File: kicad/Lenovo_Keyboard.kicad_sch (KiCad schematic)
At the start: 5 parts, among them J1 Conn_01x34_Pin, J2 Conn_01x04_Socket, J3 Conn_01x04_Socket

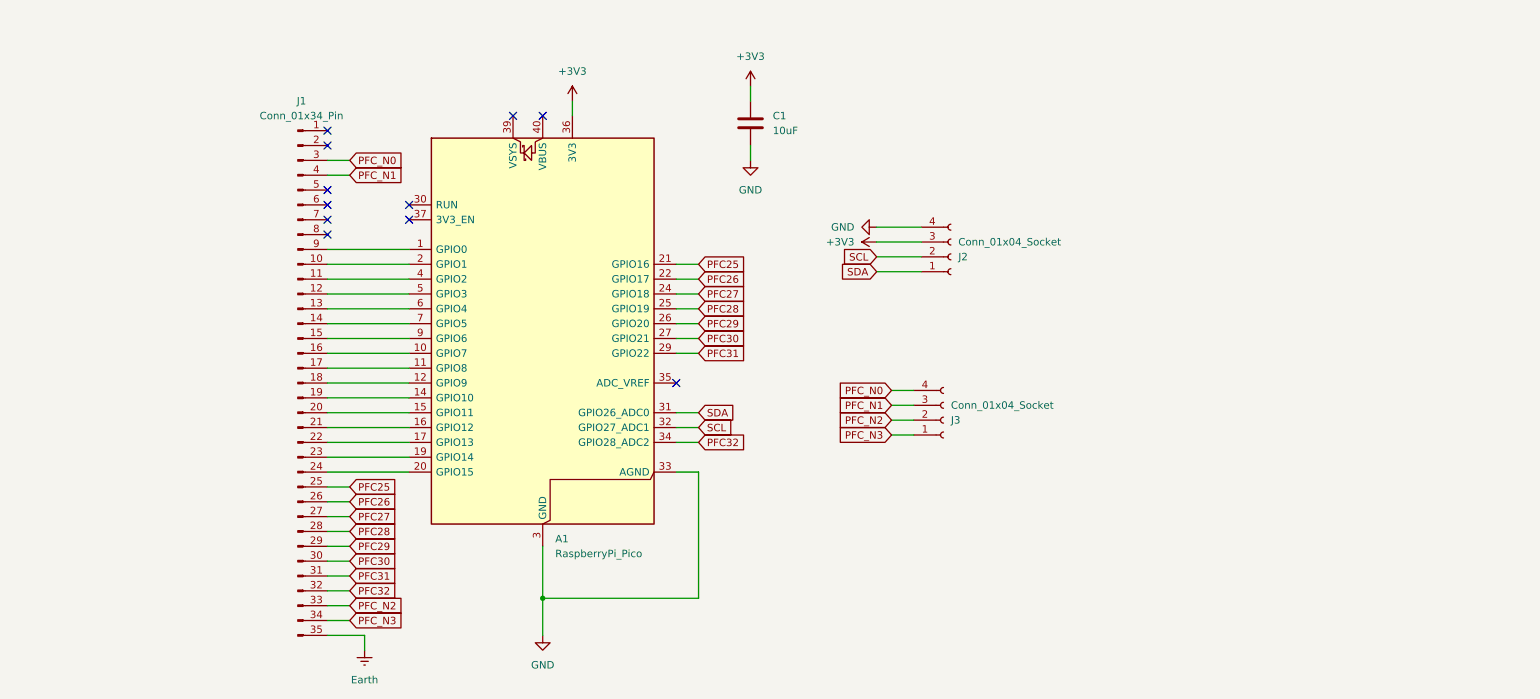
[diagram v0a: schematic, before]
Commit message: SOIC-16 version
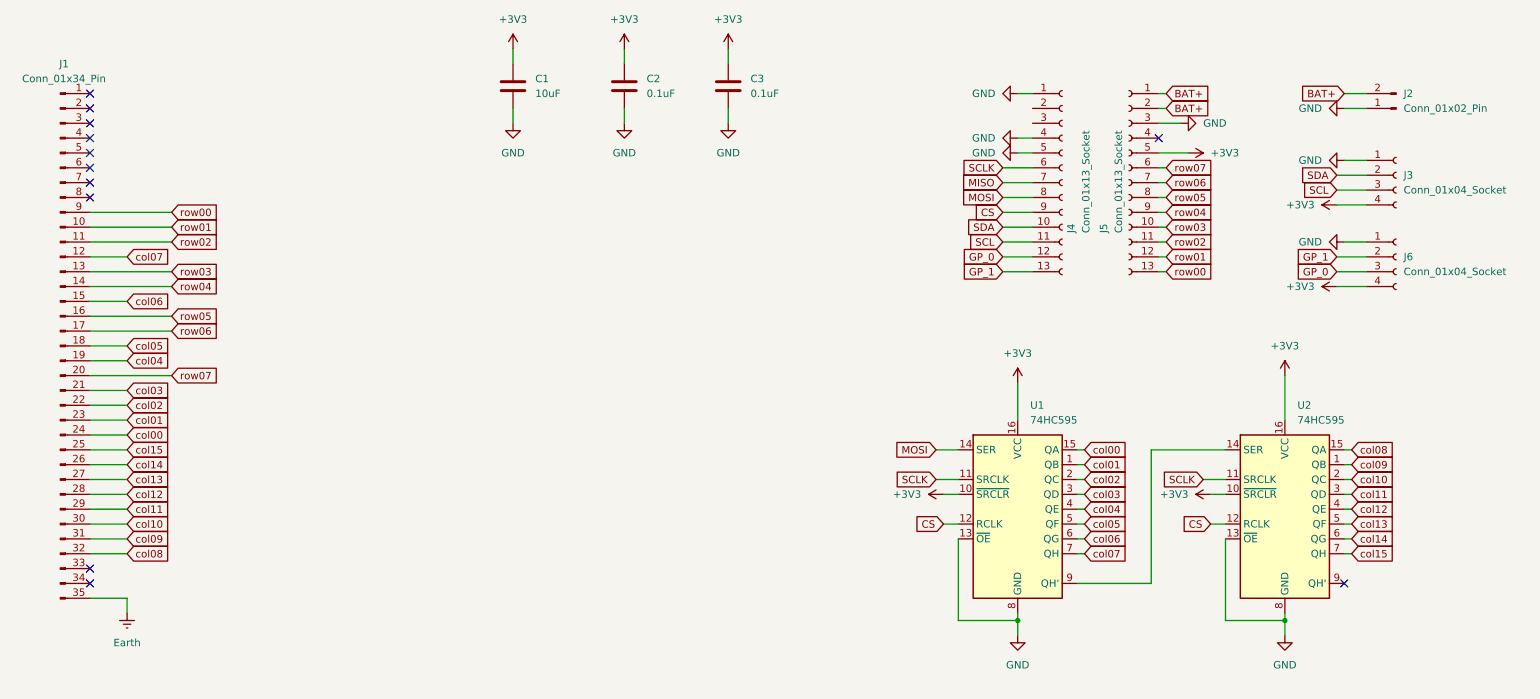
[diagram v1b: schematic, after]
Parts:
- removed A1: RaspberryPi_Pico, Module:RaspberryPi_Pico_Common_SMD, symbol MCU_Module:RaspberryPi_Pico
- removed J2: Conn_01x04_Socket, Connector_JST:JST_PH_S4B-PH-K_1x04_P2.00mm_Horizontal, symbol Connector:Conn_01x04_Socket
- added C2, C3: 0.1uF, Capacitor_SMD:C_0805_2012Metric_Pad1.18x1.45mm_HandSolder, symbol Device:C
- added J2: Conn_01x02_Pin, Connector_JST:JST_PH_S2B-PH-K_1x02_P2.00mm_Horizontal, symbol Connector:Conn_01x02_Pin
- added J4, J5: Conn_01x13_Socket, Connector_PinSocket_2.54mm:PinSocket_1x13_P2.54mm_Vertical, symbol Connector:Conn_01x13_Socket
- added J6: Conn_01x04_Socket, Connector_JST:JST_PH_S4B-PH-K_1x04_P2.00mm_Horizontal, symbol Connector:Conn_01x04_Socket
- added U1, U2: 74HC595, Package_SO:SOIC-16W_7.5x10.3mm_P1.27mm, symbol 74xx:74HC595
- J3: footprint Connector_JST:JST_ZH_B4B-ZR_1x04_P1.50mm_Vertical -> Connector_JST:JST_PH_S4B-PH-K_1x04_P2.00mm_Horizontal
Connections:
- net +3V3: now also J3.4 (Pin_4), C2.1, C3.1, J5.5 (Pin_5), J6.4 (Pin_4), U1.10 (~{SRCLR}), U1.16 (VCC), U2.10 (~{SRCLR}), U2.16 (VCC)
- net GND: now also J3.1 (Pin_1), C2.2, C3.2, J2.1 (Pin_1), J4.1 (Pin_1), J4.4 (Pin_4), J4.5 (Pin_5), J5.3 (Pin_3), J6.1 (Pin_1), U1.13 (~{OE}), U1.8 (GND), U2.13 (~{OE}), U2.8 (GND)
- net SCL: now also J3.3 (Pin_3), J4.11 (Pin_11)
- net SDA: now also J3.2 (Pin_2), J4.10 (Pin_10)
- net row00: now reaches J1.9 (Pin_9)
- net row00: now also J5.13 (Pin_13)
- net row05: now reaches J1.16 (Pin_16)
- net row05: now also J5.8 (Pin_8)
- net row06: now reaches J1.17 (Pin_17)
- net row06: now also J5.7 (Pin_7)
- net col05: now reaches J1.18 (Pin_18)
- net col05: now also U1.5 (QF)
- net col04: now reaches J1.19 (Pin_19)
- net col04: now also U1.4 (QE)
- net row07: now reaches J1.20 (Pin_20)
- net row07: now also J5.6 (Pin_6)
- net col03: now reaches J1.21 (Pin_21)
- net col03: now also U1.3 (QD)
- net col02: now reaches J1.22 (Pin_22)
- net col02: now also U1.2 (QC)
- net col01: now reaches J1.23 (Pin_23)
- net col01: now also U1.1 (QB)
- net row01: now reaches J1.10 (Pin_10)
- net row01: now also J5.12 (Pin_12)
- net col00: now reaches J1.24 (Pin_24)
- net col00: now also U1.15 (QA)
- net row02: now reaches J1.11 (Pin_11)
- net row02: now also J5.11 (Pin_11)
- net col07: now reaches J1.12 (Pin_12)
- net col07: now also U1.7 (QH)
- net row03: now reaches J1.13 (Pin_13)
- net row03: now also J5.10 (Pin_10)
- net row04: now reaches J1.14 (Pin_14)
- net row04: now also J5.9 (Pin_9)
- net col06: now reaches J1.15 (Pin_15)
- net col06: now also U1.6 (QG)
- net PFC25 renamed col15
- net col15: now also U2.7 (QH)
- net PFC26 renamed col14
- net col14: now also U2.6 (QG)
- net PFC27 renamed col13
- net col13: now also U2.5 (QF)
- net PFC28 renamed col12
- net col12: now also U2.4 (QE)
- net PFC29 renamed col11
- net col11: now also U2.3 (QD)
- net PFC30 renamed col10
- net col10: now also U2.2 (QC)
- net PFC31 renamed col09
- net col09: now also U2.1 (QB)
- net PFC32 renamed col08
- net col08: now also U2.15 (QA)
- net PFC_N0: no longer names the net of J1.3 (Pin_3)
- net PFC_N0: no longer J3.4 (Pin_4)
- net PFC_N1: no longer names the net of J1.4 (Pin_4)
- net PFC_N1: no longer J3.3 (Pin_3)
- net PFC_N2: no longer names the net of J1.33 (Pin_33)
- net PFC_N2: no longer J3.2 (Pin_2)
- net PFC_N3: no longer names the net of J1.34 (Pin_34)
- net PFC_N3: no longer J3.1 (Pin_1)
- new net: U1.9 (QH'), U2.14 (SER)
- new net BAT+: J2.2 (Pin_2), J5.1 (Pin_1), J5.2 (Pin_2)
- new net CS: J4.9 (Pin_9), U1.12 (RCLK), U2.12 (RCLK)
- new net GP_0: J4.12 (Pin_12), J6.3 (Pin_3)
- new net GP_1: J4.13 (Pin_13), J6.2 (Pin_2)
- new net MISO: J4.7 (Pin_7)
- new net MOSI: J4.8 (Pin_8), U1.14 (SER)
- new net SCLK: J4.6 (Pin_6), U1.11 (SRCLK), U2.11 (SRCLK)
- no-connect marks 11 -> 12
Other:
- moved on the sheet: C1, J1

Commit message: SOP-16 version
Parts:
- U1, U2: footprint Package_SO:SOIC-16W_7.5x10.3mm_P1.27mm -> Package_SO:SOP-16_4.4x10.4mm_P1.27mm
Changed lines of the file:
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@@
 			)
 		)
-		(property "Footprint" "Package_SO:SOIC-16W_7.5x10.3mm_P1.27mm"
+		(property "Footprint" "Package_SO:SOP-16_4.4x10.4mm_P1.27mm"
 			(at 233.68 101.6 0)
 			(effects
@@
 			)
 		)
-		(property "Footprint" "Package_SO:SOIC-16W_7.5x10.3mm_P1.27mm"
+		(property "Footprint" "Package_SO:SOP-16_4.4x10.4mm_P1.27mm"
 			(at 187.96 101.6 0)
 			(effects

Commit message: update project
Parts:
- removed J6: Conn_01x04_Socket, Connector_JST:JST_PH_S4B-PH-K_1x04_P2.00mm_Horizontal, symbol Connector:Conn_01x04_Socket
- J1: footprint Connector:FFC-PFC_0.8mm_34Pin -> 0000_Library:FFC-PFC_0.8mm_34Pin
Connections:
- net GP_0 is gone; now on net LED_ESC: J4.12 (Pin_12)
- net GP_1 is gone; now on net LED_CAPSLK: J4.13 (Pin_13)
- net GND: now also J1.3 (Pin_3), J1.33 (Pin_33)
- net LED_CAPSLK: now reaches J1.34 (Pin_34)
- net LED_ESC: now reaches J1.4 (Pin_4)
- no-connect marks 12 -> 10
